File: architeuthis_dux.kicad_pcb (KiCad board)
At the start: 2 copper layers, 122.2 x 95.6 mm, 41 parts

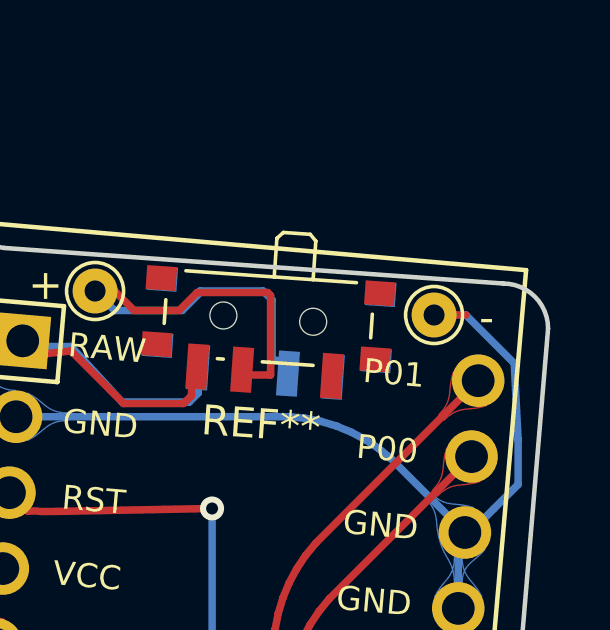
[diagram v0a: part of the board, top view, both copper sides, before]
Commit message: remove bad route
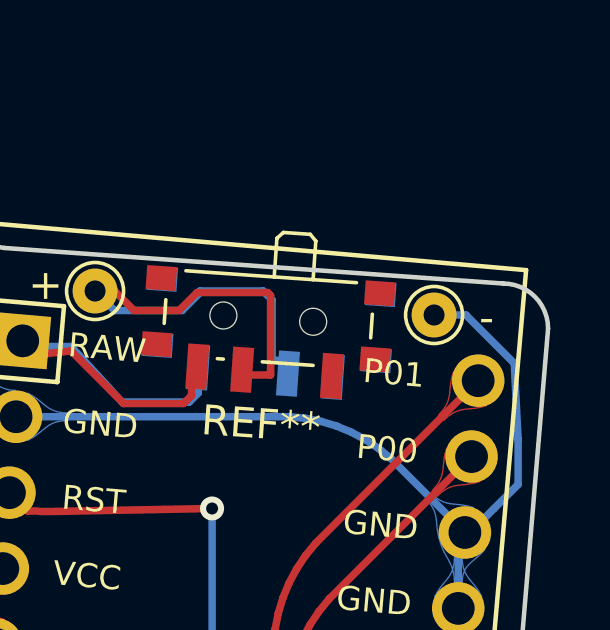
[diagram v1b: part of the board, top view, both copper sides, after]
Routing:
- net (no net): track 108.1 -> 107.1 mm
